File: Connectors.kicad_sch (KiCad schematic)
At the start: 30 parts, among them J10 LED-SWITCH, J4 124018612112A, J5 503398-1892, J6 M5-Power, J7 M5-RED, J8 Conn_01x03, J9 Feeltech, U13 USBLC6-2SC6, U14 3S Charger, U15 MAX3485

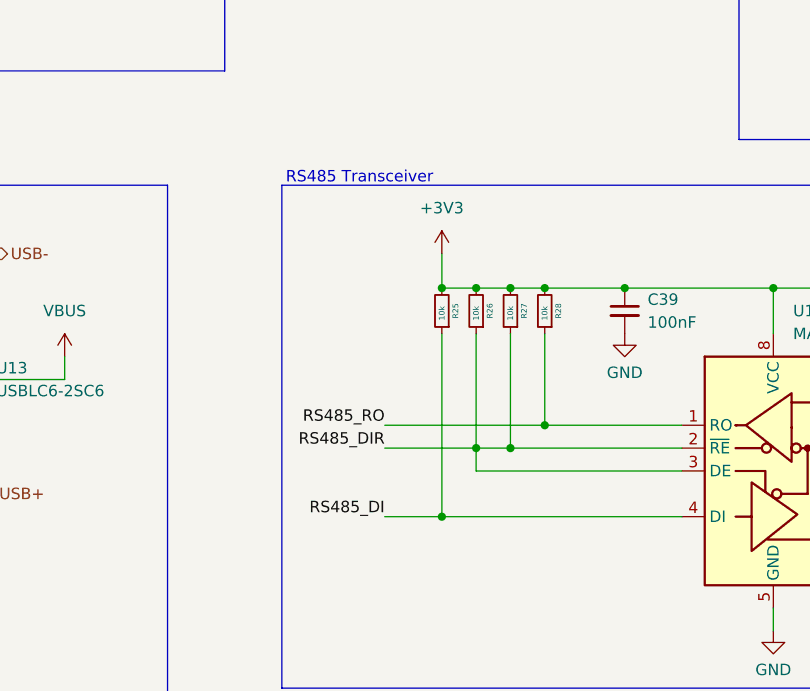
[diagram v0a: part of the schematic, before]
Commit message: Schematic updated for V2.0, updating PCB now
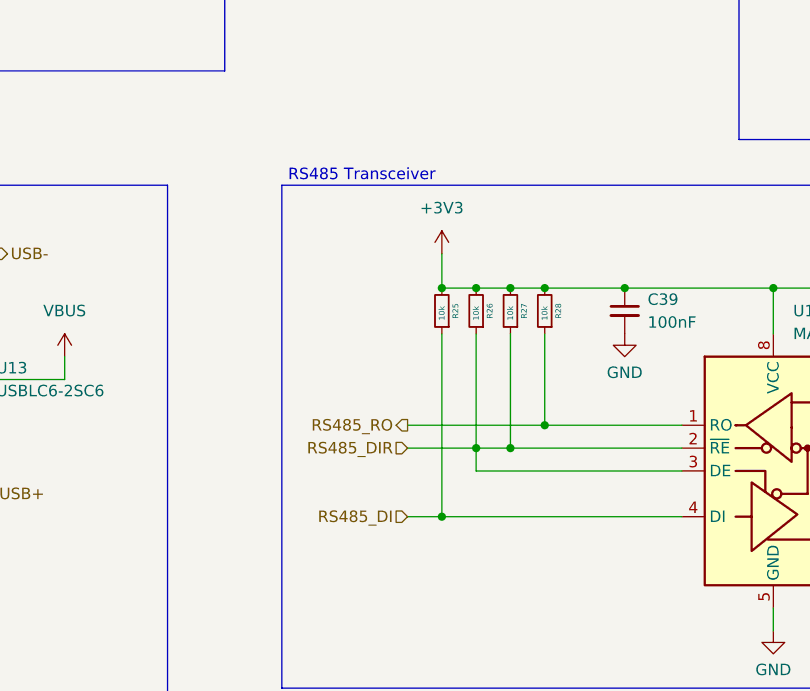
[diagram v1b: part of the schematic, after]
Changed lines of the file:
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@@
 		(title "Smart Key Cutter")
 		(date "2025-05-21")
-		(rev "1")
+		(rev "2")
 		(company "Ingenium Engineering Solutions")
 		(comment 1 "Purak Patel")
@@
 	(text "RS485 Transceiver"
 		(exclude_from_sim no)
-		(at 148.336 88.138 0)
+		(at 148.59 87.884 0)
 		(effects
 			(font
@@
 	(wire
 		(pts
-			(xy 151.13 115.57) (xy 168.91 115.57)
+			(xy 153.67 115.57) (xy 168.91 115.57)
 		)
 		(stroke
@@
 	(wire
 		(pts
-			(xy 151.13 118.11) (xy 161.29 118.11)
+			(xy 153.67 118.11) (xy 161.29 118.11)
 		)
 		(stroke
@@
 	(wire
 		(pts
-			(xy 151.13 125.73) (xy 157.48 125.73)
+			(xy 153.67 125.73) (xy 157.48 125.73)
 		)
 		(stroke
@@
 		)
 	)
-	(label "RS485_RO"
-		(at 151.13 115.57 180)
-		(effects
-			(font
-				(size 1.27 1.27)
-			)
-			(justify right bottom)
-		)
-	)
 	(label "RS485_B"
 		(at 261.62 105.41 0)
@@
 		)
 	)
-	(label "RS485_DI"
-		(at 151.13 125.73 180)
-		(effects
-			(font
-				(size 1.27 1.27)
-			)
-			(justify right bottom)
-		)
-	)
 	(label "USB_UP-"
 		(at 68.58 116.84 0)
@@
 	(label "RS485_B"
 		(at 223.52 121.92 270)
-		(effects
-			(font
-				(size 1.27 1.27)
-			)
-			(justify right bottom)
-		)
-	)
-	(label "RS485_DIR"
-		(at 151.13 118.11 180)
 		(effects
 			(font
@@
 		)
 	)
+	(hierarchical_label "RS485_RO"
+		(shape output)
+		(at 153.67 115.57 180)
+		(effects
+			(font
+				(size 1.27 1.27)
+			)
+			(justify right)
+		)
+	)
 	(hierarchical_label "I2C_SCL"
 		(shape passive)
@@
 		)
 	)
+	(hierarchical_label "RS485_DIR"
+		(shape input)
+		(at 153.67 118.11 180)
+		(effects
+			(font
+				(size 1.27 1.27)
+			)
+			(justify right)
+		)
+	)
 	(hierarchical_label "MISO"
 		(shape passive)
@@
 		(effects
 			(font
+				(size 1.27 1.27)
+			)
+			(justify right)
+		)
+	)
+	(hierarchical_label "RS485_DI"
+		(shape input)
+		(at 153.67 125.73 180)
+		(effects
+			(font

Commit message: Version 2 sent to JLC
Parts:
- removed C40: 68uF, Capacitor_SMD:C_2220_5750Metric, symbol Device:C_Small
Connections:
- net +5V: now also J8.3 (Pin_3); no longer J8.1 (Pin_1)
- net GND: now also J8.1 (Pin_1); no longer J8.3 (Pin_3)
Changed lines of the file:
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@@
 	(wire
 		(pts
+			(xy 201.93 36.83) (xy 201.93 40.64)
+		)
+		(stroke
+			(width 0)
+			(type default)
+		)
+	)
+	(wire
+		(pts
 			(xy 264.16 102.87) (xy 252.73 102.87)
 		)
@@
 	(wire
 		(pts
+			(xy 201.93 27.94) (xy 205.74 27.94)
+		)
+		(stroke
+			(width 0)
+			(type default)
+		)
+	)
+	(wire
+		(pts
 			(xy 83.82 45.72) (xy 88.9 45.72)
 		)
@@
 	(wire
 		(pts
-			(xy 259.08 110.49) (xy 259.08 100.33)
+			(xy 201.93 40.64) (xy 205.74 40.64)
 		)
 		(stroke
@@
 	(wire
 		(pts
-			(xy 274.32 105.41) (xy 274.32 104.14)
+			(xy 259.08 110.49) (xy 259.08 100.33)
 		)
 		(stroke
@@
 	(wire
 		(pts
-			(xy 201.93 30.48) (xy 201.93 31.75)
-		)
-		(stroke
-			(width 0)
-			(type default)
-		)
-	)
-	(wire
-		(pts
 			(xy 194.31 100.33) (xy 194.31 105.41)
 		)
@@
 	(wire
 		(pts
-			(xy 111.76 60.96) (xy 120.65 60.96)
+			(xy 201.93 27.94) (xy 201.93 31.75)
 		)
 		(stroke
@@
 	(wire
 		(pts
-			(xy 274.32 99.06) (xy 274.32 97.79)
+			(xy 111.76 60.96) (xy 120.65 60.96)
 		)
 		(stroke
@@
 	(wire
 		(pts
-			(xy 201.93 38.1) (xy 201.93 36.83)
-		)
-		(stroke
-			(width 0)
-			(type default)
-		)
-	)
-	(wire
-		(pts
 			(xy 31.75 57.15) (xy 31.75 54.61)
 		)
@@
 	)
 	(symbol
-		(lib_id "power:+BATT")
-		(at 274.32 97.79 0)
-		(unit 1)
-		(exclude_from_sim no)
-		(in_bom yes)
-		(on_board yes)
-		(dnp no)
-		(property "Reference" "#PWR0103"
-			(at 274.32 101.6 0)
-			(effects
-				(font
-					(size 1.27 1.27)
-				)
-				(hide yes)
-			)
-		)
-		(property "Value" "+BATT"
-			(at 274.066 94.234 0)
-			(effects
-				(font
-					(size 1.27 1.27)
-				)
-			)
-		)
-		(property "Footprint" ""
-			(at 274.32 97.79 0)
-			(effects
-				(font
-					(size 1.27 1.27)
-				)
-				(hide yes)
-			)
-		)
-		(property "Datasheet" ""
-			(at 274.32 97.79 0)
-			(effects
-				(font
-					(size 1.27 1.27)
-				)
-				(hide yes)
-			)
-		)
-		(property "Description" "Power symbol creates a global label with name \"+BATT\""
-			(at 274.32 97.79 0)
-			(effects
-				(font
-					(size 1.27 1.27)
-				)
-				(hide yes)
-			)
-		)
-		(pin "1"
-		)
-		(instances
-			(project "Smart Key Cutter Interface"
-				(path "/e7f6820c-98d8-4aa2-b050-9c8bdbf7cc14/8038a708-9059-498f-8abf-317776704634"
-					(reference "#PWR0103")
-					(unit 1)
-				)
-			)
-		)
-	)
-	(symbol
 		(lib_id "power:VBUS")
 		(at 115.57 107.95 0)
@@
 	(symbol
 		(lib_id "power:GND")
-		(at 201.93 38.1 0)
+		(at 205.74 27.94 0)
 		(unit 1)
 		(exclude_from_sim no)
@@
 		(dnp no)
 		(property "Reference" "#PWR096"
-			(at 201.93 44.45 0)
+			(at 205.74 34.29 0)
 			(effects
 				(font
@@
 		)
 		(property "Value" "GND"
-			(at 201.93 41.91 0)
+			(at 205.74 31.75 0)
 			(effects
 				(font
@@
 		)
 		(property "Footprint" ""
-			(at 201.93 38.1 0)
+			(at 205.74 27.94 0)
 			(effects
 				(font
@@
 		)
 		(property "Datasheet" ""
-			(at 201.93 38.1 0)
+			(at 205.74 27.94 0)
 			(effects
 				(font
@@
 		)
 		(property "Description" "Power symbol creates a global label with name \"GND\" , ground"
-			(at 201.93 38.1 0)
+			(at 205.74 27.94 0)
 			(effects
 				(font
@@
 	)
 	(symbol
-		(lib_id "power:GND")
-		(at 274.32 105.41 0)
-		(unit 1)
-		(exclude_from_sim no)
-		(in_bom yes)
-		(on_board yes)
-		(dnp no)
-		(property "Reference" "#PWR0104"
-			(at 274.32 111.76 0)
-			(effects
-				(font
-					(size 1.27 1.27)
-				)
-				(hide yes)
-			)
-		)
-		(property "Value" "GND"
-			(at 274.32 109.728 0)
-			(effects
-				(font
-					(size 1.27 1.27)
-				)
-			)
-		)
-		(property "Footprint" ""
-			(at 274.32 105.41 0)
-			(effects
-				(font
-					(size 1.27 1.27)
-				)
-				(hide yes)
-			)
-		)
-		(property "Datasheet" ""
-			(at 274.32 105.41 0)
-			(effects
-				(font
-					(size 1.27 1.27)
-				)
-				(hide yes)
-			)
-		)
-		(property "Description" "Power symbol creates a global label with name \"GND\" , ground"
-			(at 274.32 105.41 0)
-			(effects
-				(font
-					(size 1.27 1.27)
-				)
-				(hide yes)
-			)
-		)
-		(pin "1"
-		)
-		(instances
-			(project "Smart Key Cutter Interface"
-				(path "/e7f6820c-98d8-4aa2-b050-9c8bdbf7cc14/8038a708-9059-498f-8abf-317776704634"
-					(reference "#PWR0104")
-					(unit 1)
-				)
-			)
-		)
-	)
-	(symbol
 		(lib_id "Device:R_Small")
 		(at 161.29 102.87 180)
@@
 	(symbol
 		(lib_id "power:+5V")
-		(at 201.93 30.48 0)
+		(at 205.74 40.64 0)
 		(unit 1)
 		(exclude_from_sim no)
@@
 		(dnp no)
 		(property "Reference" "#PWR095"
-			(at 201.93 34.29 0)
+			(at 205.74 44.45 0)
 			(effects
 				(font
@@
 		)
 		(property "Value" "+5V"
-			(at 201.93 26.924 0)
+			(at 205.74 37.084 0)
 			(effects
 				(font
@@
 		)
 		(property "Footprint" ""
-			(at 201.93 30.48 0)
+			(at 205.74 40.64 0)
 			(effects
 				(font
@@
 		)
 		(property "Datasheet" ""
-			(at 201.93 30.48 0)
+			(at 205.74 40.64 0)
 			(effects
 				(font
@@
 		)
 		(property "Description" "Power symbol creates a global label with name \"+5V\""
-			(at 201.93 30.48 0)
+			(at 205.74 40.64 0)
 			(effects
 				(font
@@
 					(unit 1)
 				)
-			)
-		)
-	)
-	(symbol
-		(lib_id "Device:C_Small")
-		(at 274.32 101.6 0)
-		(mirror y)
-		(unit 1)
-		(exclude_from_sim no)
-		(in_bom yes)
-		(on_board yes)
-		(dnp no)
-		(property "Reference" "C40"
-			(at 271.526 101.6 0)
-			(effects
-				(font
-					(size 0.635 0.635)
-				)
-			)
-		)
-		(property "Value" "68uF"
-			(at 277.622 101.6 0)
-			(effects
-				(font
-					(size 0.635 0.635)
-				)
-			)
-		)
-		(property "Footprint" "Capacitor_SMD:C_2220_5750Metric"
-			(at 274.32 101.6 0)
-			(effects
-				(font
-					(size 1.27 1.27)
-				)
-				(hide yes)
-			)
-		)
-		(property "Datasheet" "~"
-			(at 274.32 101.6 0)
-			(effects
-				(font
-					(size 1.27 1.27)
-				)
-				(hide yes)
-			)
-		)
-		(property "Description" "Unpolarized capacitor, small symbol"
-			(at 274.32 101.6 0)
-			(effects
-				(font
-					(size 1.27 1.27)
-				)
-				(hide yes)
-			)
-		)
-		(property "JLCPCB Part #" "C342299"
-			(at 274.32 101.6 0)
-			(effects
-				(font
-					(size 1.27 1.27)
-				)
-				(hide yes)
-			)
-		)
-		(pin "1"
-		)
-		(pin "2"
-		)
-		(instances
-			(project "Smart Key Cutter Interface"
-				(path "/e7f6820c-98d8-4aa2-b050-9c8bdbf7cc14/8038a708-9059-498f-8abf-317776704634"
-					(reference "C40")
-					(unit 1)
-				)
